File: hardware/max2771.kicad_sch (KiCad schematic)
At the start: 23 parts, among them IC7 MAX2771ETI+

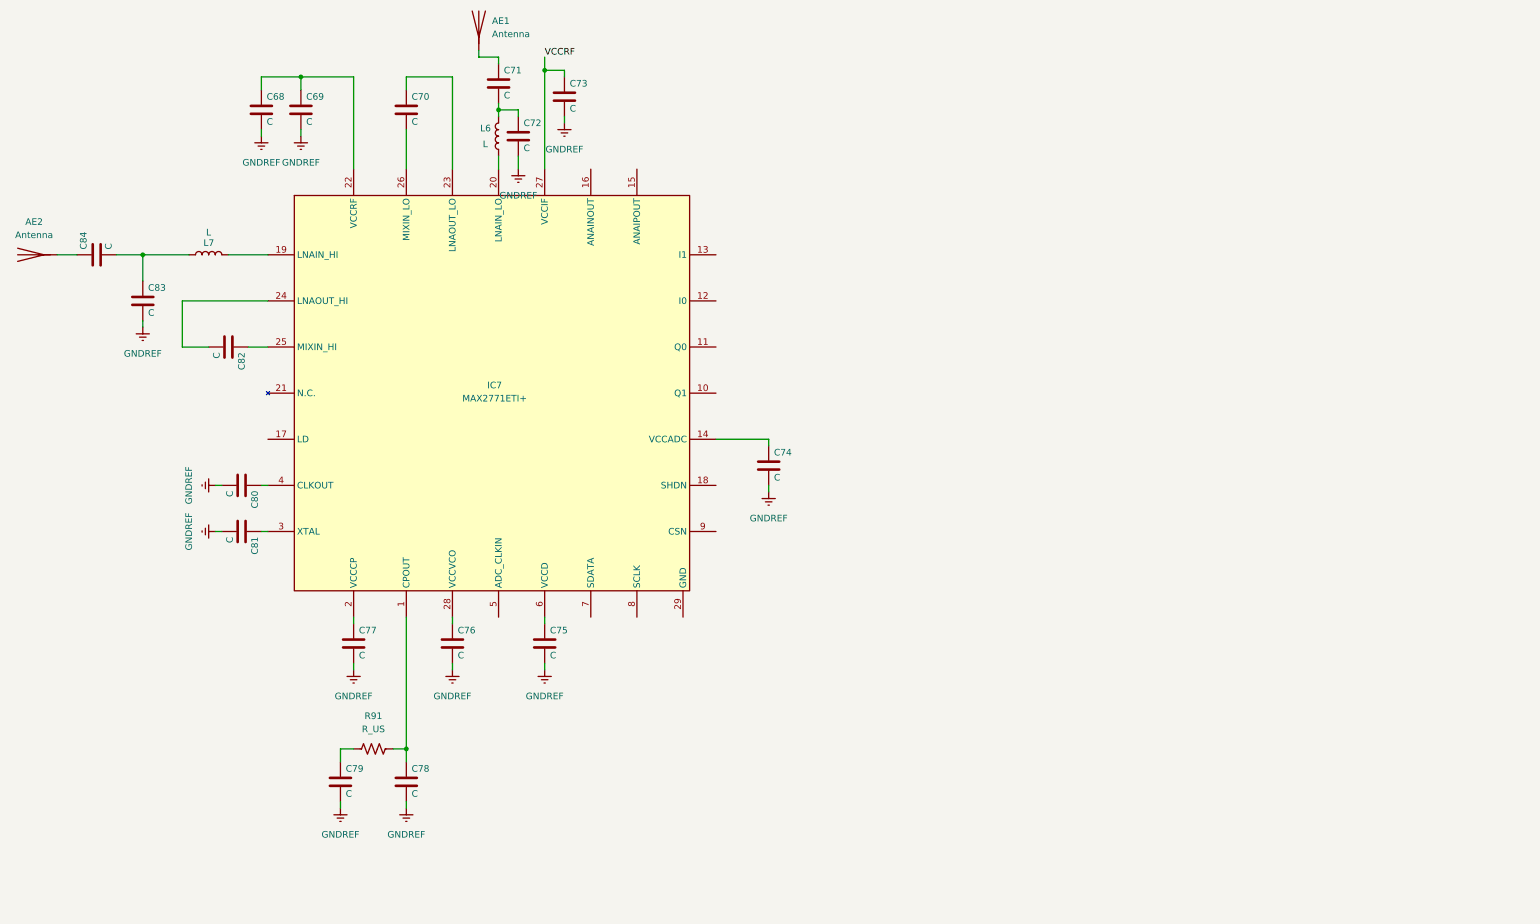
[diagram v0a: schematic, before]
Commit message: update schematic
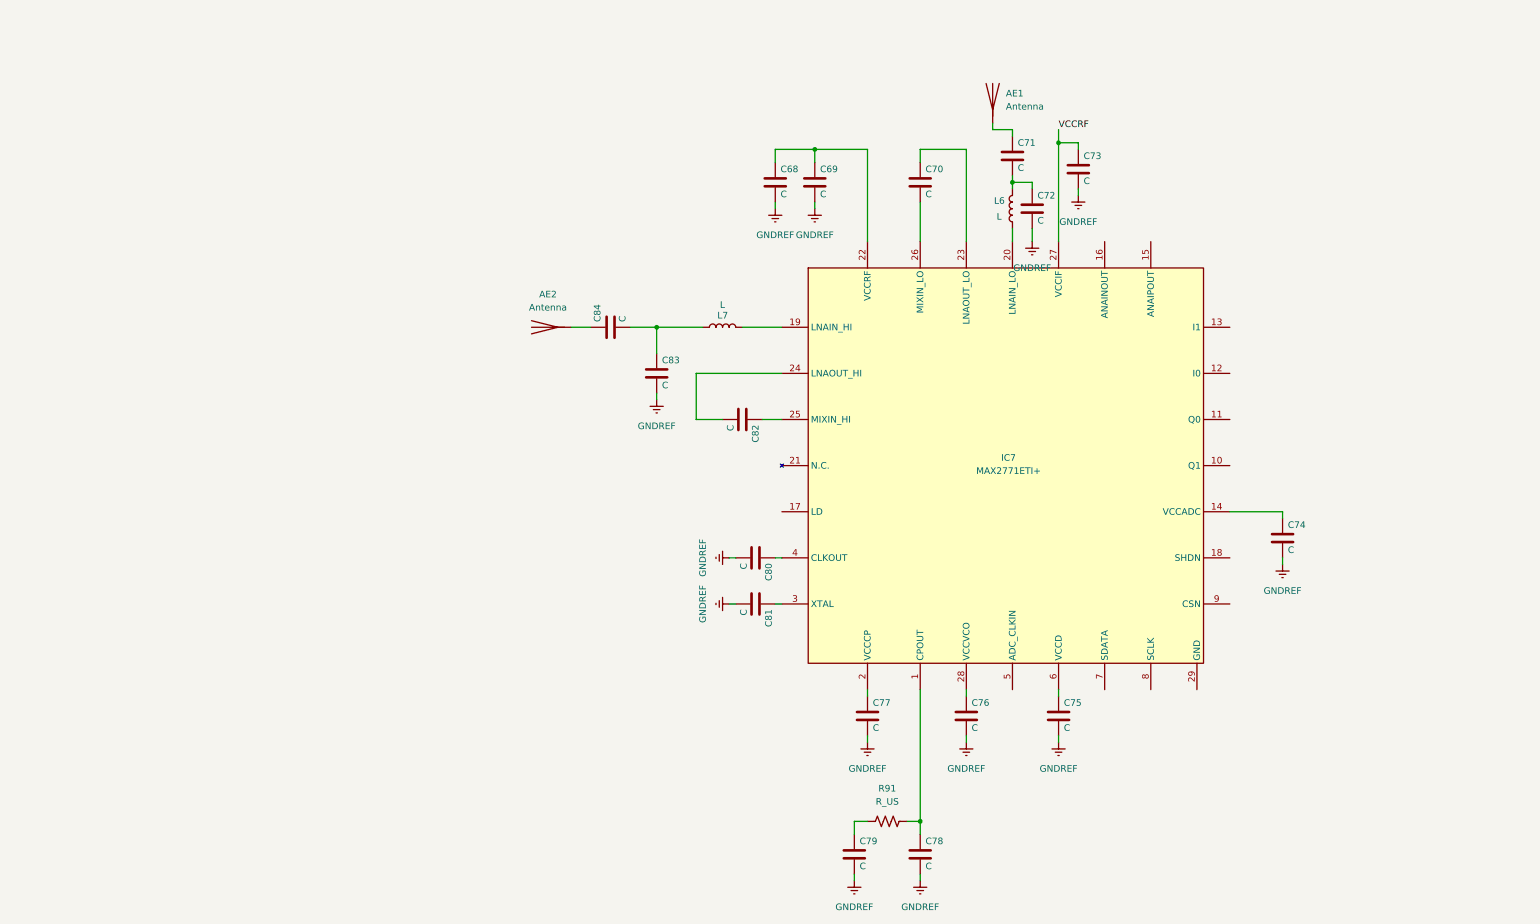
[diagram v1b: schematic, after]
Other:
- moved on the sheet: AE1, AE2, C68, C69, C70, C71, C72, C73, C74, C75, C76, C77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

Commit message: updated schematic
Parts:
- removed AE1, AE2: Antenna, symbol Device:Antenna
- removed C70, C71, C72, C73, C74, C75, C76, C77, C78, C79, C80, C81, C82, C83, C84: C, symbol Device:C
- removed L6, L7: L, symbol Device:L
- removed R91: R_US, symbol Device:R_US
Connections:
- net GNDREF: now also C68.2, C69.2, IC7.29 (GND); no longer C68.1, C69.1
- net VCC_ADC: now reaches IC7.14 (VCCADC)
- net VCC_ADC: now also C68.1, C69.1
- net ANAIPOUT: now reaches IC7.15 (ANAIPOUT)
- net ANAINOUT: now reaches IC7.16 (ANAINOUT)
- net CLK_OUT: now reaches IC7.4 (CLKOUT)
- net ADC_CLKIN: now reaches IC7.5 (ADC_CLKIN)
- net SPI_DATA: now reaches IC7.7 (SDATA)
- net SPI_CLK: now reaches IC7.8 (SCLK)
- net SPI_CSN: now reaches IC7.9 (CSN)
- net VCCRF: no longer names the net of IC7.27 (VCCIF)
- now unconnected: IC7.22 (VCCRF)
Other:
- moved on the sheet: IC7
